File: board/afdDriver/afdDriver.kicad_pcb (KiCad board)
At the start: 2 copper layers, 43.2 x 58.4 mm, 58 parts, among them J1 Qwiic_Connector, J2 Qwiic_Connector, J3 HighVoltageAC, J4 HighVoltageAC, J5 Power, U1 PCF8574TS, U2 QTM3063T1, U3 QTM3063T1, U4 QTM3063T1, U5 QTM3063T1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

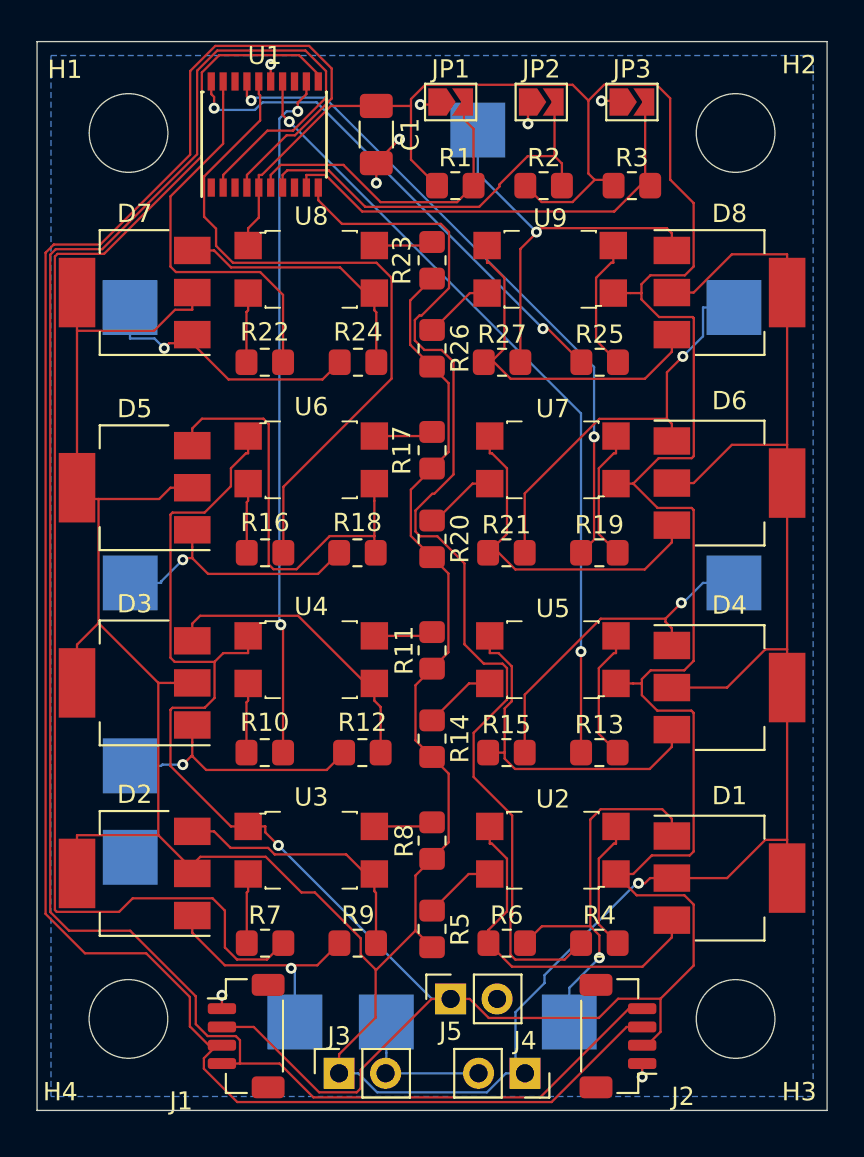
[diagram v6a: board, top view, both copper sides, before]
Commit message: Embiggened +5V net.
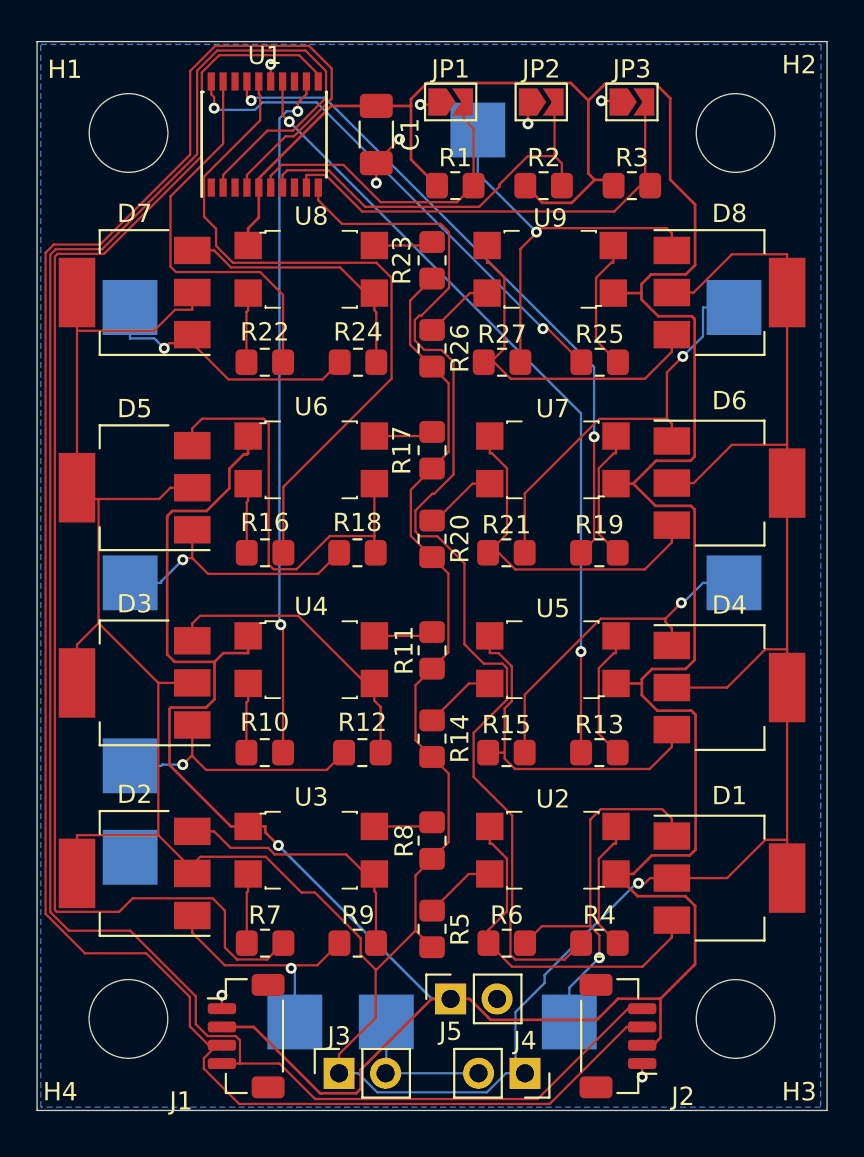
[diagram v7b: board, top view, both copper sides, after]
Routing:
- net +5V: track 201.3 -> 202.6 mm
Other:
- board text added: "V1.0.0"
